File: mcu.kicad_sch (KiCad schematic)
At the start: 8 parts, among them U1 113991054

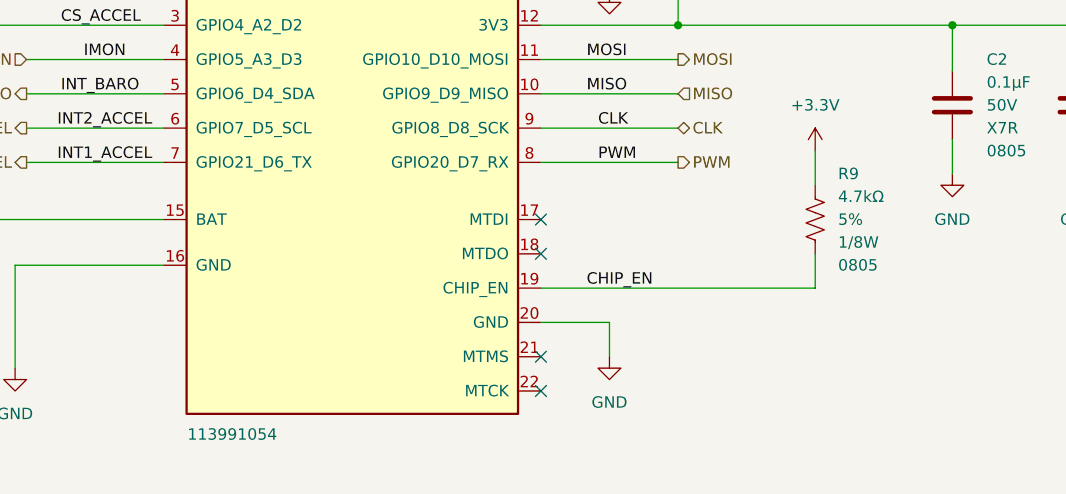
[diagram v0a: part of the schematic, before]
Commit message: Removed duplicate pullup on chip enable resistor
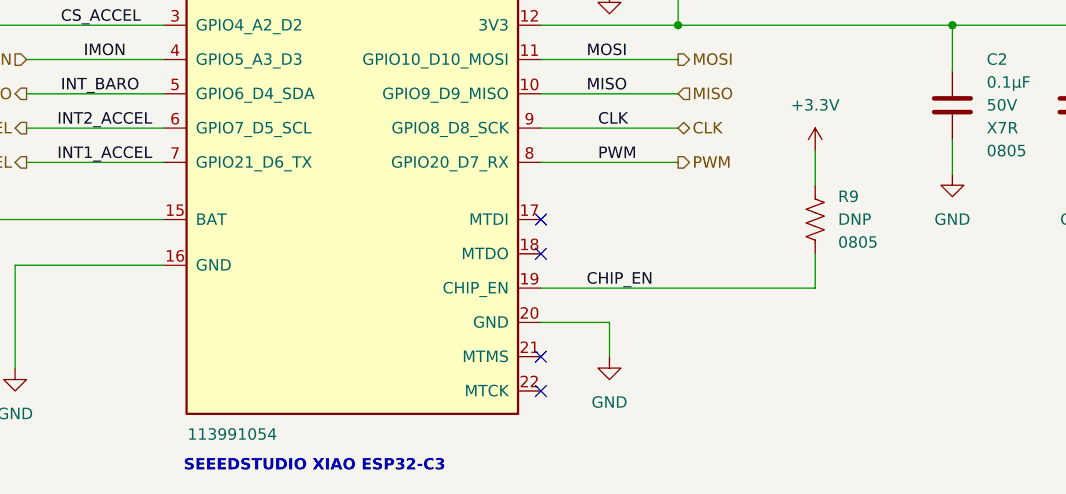
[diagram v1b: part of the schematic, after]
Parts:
- removed R9: RMCF0805JT4K70, Resistor_SMD:R_0805_2012Metric_Pad1.20x1.40mm_HandSolder, symbol Resistors:RMCF0805JT4K70
- added R9: DNP 0805, Resistor_SMD:R_0805_2012Metric_Pad1.20x1.40mm_HandSolder, symbol Resistors:DNP_0805
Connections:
- net +3.3V: now also R9.1
- net CHIP_EN: now also R9.2
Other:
- note added: "SEEEDSTUDIO XIAO ESP32-C3"
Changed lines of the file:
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@@
+		)
+	)
+	(text "SEEEDSTUDIO XIAO ESP32-C3\n"
+		(exclude_from_sim no)
+		(at 139.954 126.492 0)
+		(effects
+			(font
+				(size 1.27 1.27)
+				(thickness 0.254)
+				(bold yes)
+			)
 		)
 	)
@@
 			)
 			(justify left)
+		)
+	)
+	(symbol
+		(lib_id "Resistors:DNP_0805")
+		(at 195.58 99.06 0)
+		(unit 1)
+		(exclude_from_sim no)
+		(in_bom yes)
+		(on_board yes)
+		(dnp no)
+		(fields_autoplaced yes)
+		(property "Reference" "R9"
+			(at 198.12 96.5199 0)
+			(effects
+				(font
+					(size 1.27 1.27)
+				)
+				(justify left)
+			)
+		)
+		(property "Value" "DNP 0805"
+			(at 198.882 113.284 0)
+			(effects
+				(font
+					(size 1.27 1.27)
+				)
+				(justify left bottom)
+				(hide yes)
+			)
+		)
+		(property "Footprint" "Resistor_SMD:R_0805_2012Metric_Pad1.20x1.40mm_HandSolder"
+			(at 196.596 120.65 0)
+			(effects
+				(font
+					(size 1.27 1.27)
+				)
+				(justify bottom)
+				(hide yes)
+			)
+		)
+		(property "Datasheet" ""
+			(at 195.58 99.06 90)
+			(effects
+				(font
+					(size 1.27 1.27)
+				)
+				(hide yes)
+			)
+		)
+		(property "Description" "Res 0805 Do Not Populate"
+			(at 196.342 117.856 0)
+			(effects
+				(font
+					(size 1.27 1.27)
+				)
+				(hide yes)
+			)
+		)
+		(property "PARTREV" "V.12"
+			(at 204.47 123.19 0)
+			(effects
+				(font
+					(size 1.27 1.27)
+				)
+				(justify bottom)
+				(hide yes)
+			)
+		)
+		(property "STANDARD" "IPC 7351B"
+			(at 196.088 123.19 0)
+			(effects
+				(font
+					(size 1.27 1.27)
+				)
+				(justify bottom)
+				(hide yes)
+			)
+		)
+		(property "MAXIMUM_PACKAGE_HEIGHT" "0.6 mm"
+			(at 186.182 123.19 0)
+			(effects
+				(font
+					(size 1.27 1.27)
+				)
+				(justify bottom)
+				(hide yes)
+			)
+		)
+		(property "MANUFACTURER" "Yageo"
+			(at 195.834 116.84 0)
+			(effects
+				(font
+					(size 1.27 1.27)
+				)
+				(justify bottom)
+				(hide yes)
+			)
+		)
+		(property "Resistance" "DNP"
+			(at 198.12 99.0599 0)
+			(effects
+				(font
+					(size 1.27 1.27)
+				)
+				(justify left)
+			)
+		)
+		(property "Tolerance" "-"
+			(at 195.58 125.222 0)
+			(effects
+				(font
+					(size 1.27 1.27)
+				)
+				(justify left)
+				(hide yes)
+			)
+		)
+		(property "Power" "1/8W"
+			(at 195.326 124.206 0)
+			(effects
+				(font
+					(size 1.27 1.27)
+				)
+				(justify left)
+				(hide yes)
+			)
+		)
+		(property "Package" "0805"
+			(at 198.12 101.5999 0)
+			(effects
+				(font
+					(size 1.27 1.27)
+				)
+				(justify left)
+			)
+		)
+		(pin "2"
+		)
+		(pin "1"
+		)
+		(instances
+			(project ""
+				(path "/c7c1fa07-b1f1-4333-8175-bf8c0499ed8b/c1b40844-8219-482d-890b-f526596d823e"
+					(reference "R9")
+					(unit 1)
+				)
+			)
 		)
 	)
@@
 					(unit 1)
 				)
-			)
-		)
-	)
-	(symbol
-		(lib_id "Resistors:RMCF0805JT4K70")
-		(at 195.58 99.06 0)
-		(unit 1)
-		(exclude_from_sim no)
-		(in_bom yes)
-		(on_board yes)
-		(dnp no)
-		(fields_autoplaced yes)
-		(property "Reference" "R9"
-			(at 198.12 93.9799 0)
-			(effects
-				(font
-					(size 1.27 1.27)
-				)
-				(justify left)
-			)
-		)
-		(property "Value" "RMCF0805JT4K70"
-			(at 207.518 124.968 0)
-			(effects
-				(font
-					(size 1.27 1.27)
-				)
-				(justify left bottom)
-				(hide yes)
-			)
-		)
-		(property "Footprint" "Resistor_SMD:R_0805_2012Metric_Pad1.20x1.40mm_HandSolder"
-			(at 196.596 120.65 0)
-			(effects
-				(font
-					(size 1.27 1.27)
-				)
-				(justify bottom)
-				(hide yes)
-			)
-		)
-		(property "Datasheet" ""
-			(at 195.58 99.06 90)
-			(effects
-				(font
-					(size 1.27 1.27)
-				)
-				(hide yes)
-			)
-		)
-		(property "Description" "RES 4.7K OHM 5% 1/8W 0805"
-			(at 196.342 117.856 0)
-			(effects
-				(font
-					(size 1.27 1.27)
-				)
-				(hide yes)
-			)
-		)
-		(property "PARTREV" "V.12"
-			(at 204.47 123.19 0)
-			(effects
-				(font
-					(size 1.27 1.27)
-				)
-				(justify bottom)
-				(hide yes)
-			)
-		)
-		(property "STANDARD" "IPC 7351B"
-			(at 196.088 123.19 0)
-			(effects
-				(font
-					(size 1.27 1.27)
-				)
-				(justify bottom)
-				(hide yes)
-			)
-		)
-		(property "MAXIMUM_PACKAGE_HEIGHT" "0.6 mm"
-			(at 186.182 123.19 0)
-			(effects
-				(font
-					(size 1.27 1.27)
-				)
-				(justify bottom)
-				(hide yes)
-			)
-		)
-		(property "MANUFACTURER" "Yageo"
-			(at 195.834 116.84 0)
-			(effects
-				(font
-					(size 1.27 1.27)
-				)
-				(justify bottom)
-				(hide yes)
-			)
-		)
-		(property "Resistance" "4.7kΩ"
-			(at 198.12 96.5199 0)
-			(effects
-				(font
-					(size 1.27 1.27)
-				)
-				(justify left)
-			)
-		)
-		(property "Tolerance" "5%"
-			(at 198.12 99.0599 0)
-			(effects
-				(font
-					(size 1.27 1.27)
-				)
-				(justify left)
-			)
-		)
-		(property "Power" "1/8W"
-			(at 198.12 101.5999 0)
-			(effects
-				(font
-					(size 1.27 1.27)
-				)
-				(justify left)
-			)
-		)
-		(property "Package" "0805"
-			(at 198.12 104.1399 0)
-			(effects
-				(font
-					(size 1.27 1.27)
-				)
-				(justify left)
-			)
-		)
-		(pin "2"
-		)
-		(pin "1"
-		)
-		(instances
-			(project "Spa-Raidillon"
-				(path "/c7c1fa07-b1f1-4333-8175-bf8c0499ed8b/c1b40844-8219-482d-890b-f526596d823e"
-					(reference "R9")
-					(unit 1)
-				)

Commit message: ordered pcb
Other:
- title: (none) -> Radillon
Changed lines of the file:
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@@
 	(generator_version "8.0")
 	(paper "A4")
+	(title_block
+		(title "Radillon")
+		(date "2025-01-29")
+		(rev "1")
+	)
 	(junction
 		(at 210.82 77.47)
